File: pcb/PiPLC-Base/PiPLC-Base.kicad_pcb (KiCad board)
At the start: 2 copper layers, 158 x 85 mm, 144 parts, among them J1 WJ2EDGRC-5.08-4P, J10 WJ2EDGRC-5.08-4P, J11 WJ2EDGRC-5.08-4P, J12 WJ2EDGRC-5.08-4P, J13 ?, J2 KNX, J3 WJ2EDGRC-5.08-4P, J4 WJ2EDGRC-5.08-4P, J5 WJ2EDGRC-5.08-4P, J6 WJ2EDGRC-5.08-4P, J7 WJ2EDGRC-5.08-4P, J8 WJ2EDGRC-5.08-4P, J9 WJ2EDGRC-5.08-4P, J99 Rpi GPIO, K1 G5RL-1A-E-TV8 DC24, K2 G5RL-1A-E-TV8 DC24, K3 G5RL-1A-E-TV8 DC24, K4 G5RL-1A-E-TV8 DC24, K5 G5RL-1A-E-TV8 DC24, K6 G5RL-1A-E-TV8 DC24, K7 G5RL-1A-E-TV8 DC24, K8 G5RL-1A-E-TV8 DC24, Q1 AO3400A, Q2 AO3400A, Q3 AO3400A, Q4 AO3400A, Q5 AO3400A, Q6 AO3400A, Q7 AO3400A, Q8 AO3400A, U1 TPS54331D, U10 EL817C, U11 EL817C, U2 NCN5121, U3 ISO1540, U4 EL817C, U5 EL817C, U6 EL817C, U7 EL817C, U8 EL817C, U9 EL817C, Y1 16MHz

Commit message: Move stuff on both PCBs for 3D proof of concept
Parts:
- removed D10, D11, D20, D21, D22, D23, D24, D25, D26, D27, D4, D5, D6, D7, D8, D9: LED, LED_THT:LED_D5.0mm
- removed J2: KNX, MeineBib:KNX_Header
- moved C6 32.4 mm to (58.7, 143.3)
- moved C7 32.4 mm to (58.7, 146.6)
- moved C1 32.4 mm to (-9.28, 130.1)
- moved C10 32.4 mm to (49.9, 151.3)
- moved C11 32.4 mm to (-9.28, 147.7)
- moved C12 32.4 mm to (-9.28, 150.2)
- moved C13 32.4 mm to (-9.28, 152.7)
- moved C14 32.4 mm to (-5.27, 130.1)
- moved C15 32.4 mm to (24.3, 132.9)
- moved C16 32.4 mm to (24.2, 141.5)
- moved C2 32.4 mm to (-9.28, 132.6)
- moved C3 32.4 mm to (-9.28, 135.1)
- moved C4 32.4 mm to (-9.28, 137.6)
- moved C5 32.4 mm to (-9.28, 140.1)
- moved C8 32.4 mm to (-9.28, 142.7)
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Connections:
- net /GPIO_02 renamed I²C SDA
- net /GPIO_03 renamed I²C SCL
- net GND renamed KNX -
- net Net-(D2-A) renamed KNX +
- R16 pad 1: Net-(D4-A) -> /GPIO_09
- R16 pad 2: +3V3 -> LED_I5
- R17 pad 1: Net-(D5-A) -> /GPIO_11
- R17 pad 2: +3V3 -> LED_I6
- R18 pad 1: Net-(D6-A) -> /GPIO_05
- R18 pad 2: +3V3 -> LED_I7
- R19 pad 1: Net-(D7-A) -> /GPIO_06
- R19 pad 2: +3V3 -> LED_I8
- R20 pad 1: Net-(D8-A) -> /GPIO_17
- R20 pad 2: +3V3 -> LED_I1
- R21 pad 1: Net-(D9-A) -> /GPIO_27
- R21 pad 2: +3V3 -> LED_I2
- R22 pad 1: Net-(D10-A) -> /GPIO_22
- R22 pad 2: +3V3 -> LED_I3
- R23 pad 1: Net-(D11-A) -> /GPIO_10
- R23 pad 2: +3V3 -> LED_I4
- R25 pad 1: Net-(D21-A) -> LED_Q2
- R27 pad 1: Net-(D22-A) -> LED_Q3
- R30 pad 1: Net-(D23-A) -> LED_Q4
- R33 pad 1: Net-(D24-A) -> LED_Q5
- R36 pad 1: Net-(D25-A) -> LED_Q6
- R39 pad 1: Net-(D26-A) -> LED_Q7
- R42 pad 1: Net-(D27-A) -> LED_Q8
- R48 pad 1: Net-(D20-A) -> LED_Q1

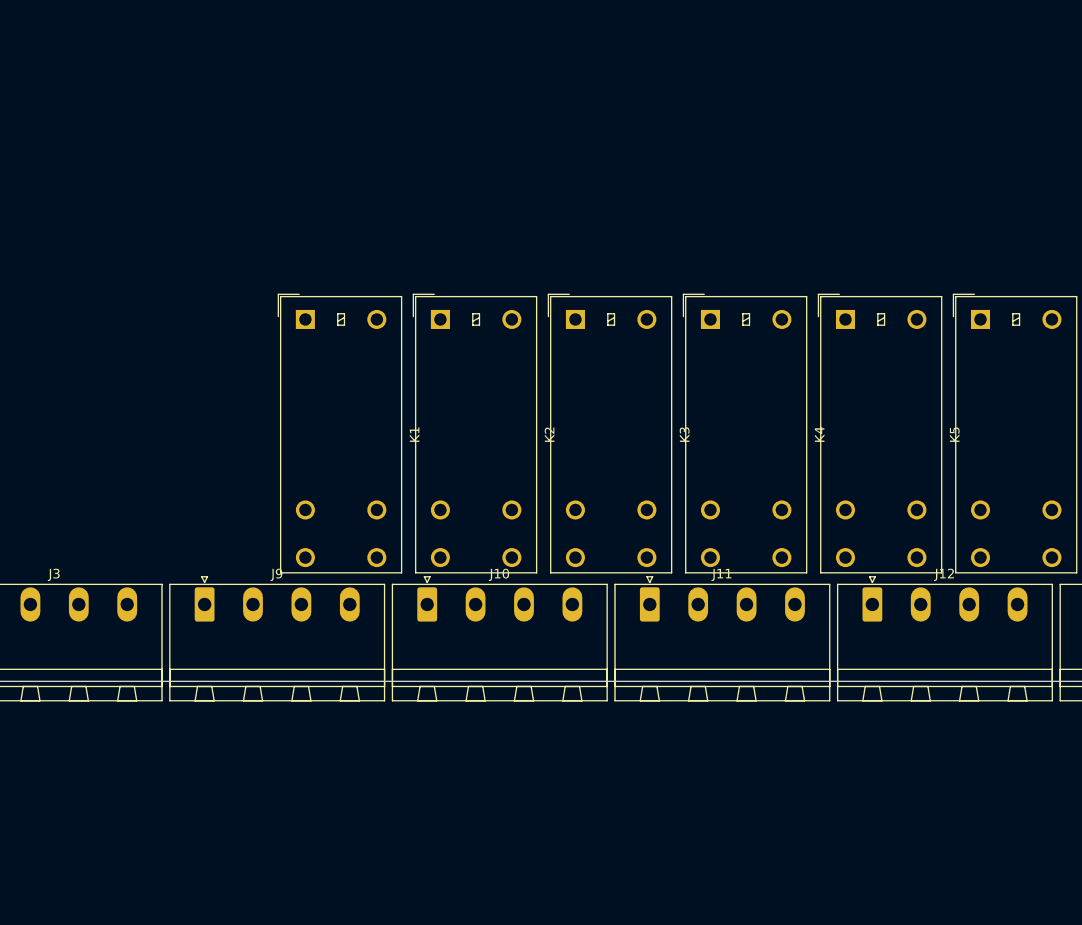
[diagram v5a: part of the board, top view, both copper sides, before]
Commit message: Add Modbus
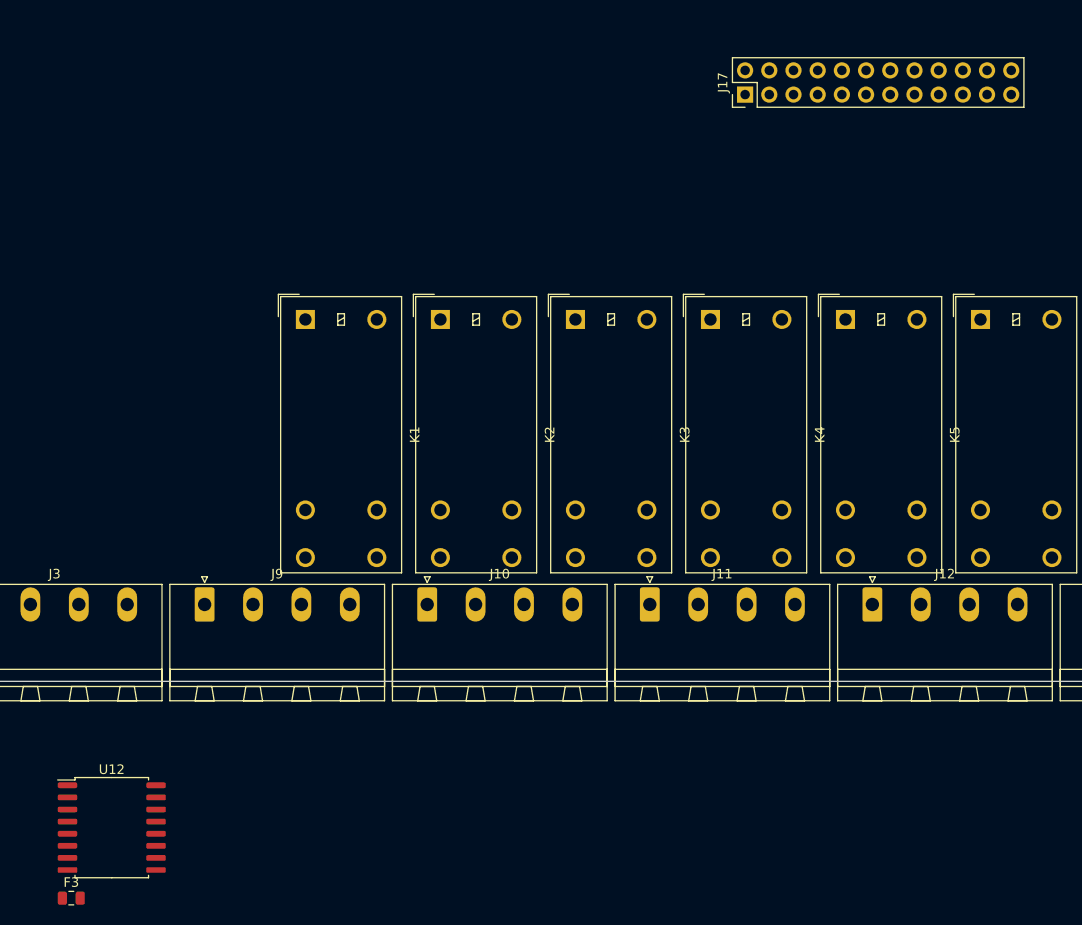
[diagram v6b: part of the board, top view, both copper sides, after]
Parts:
- added F3: 500mA, Fuse:Fuse_0805_2012Metric, F.Cu at (88.3, 171.3)
- added J17: Conn_02x12_Odd_Even, Connector_PinHeader_2.54mm:PinHeader_2x12_P2.54mm_Vertical, F.Cu at (159.0, 86.9)
- added U12: ISO3082DWR, Package_SO:SOIC-16W_7.5x10.3mm_P1.27mm, F.Cu at (92.5, 163.9)
- J13: value ? -> Modbus
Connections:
- J13 pad 1: /GPIO_13 -> Net-(J13-Pin_1)
- J13 pad 2: /GPIO_19 -> Net-(J13-Pin_2)
- J13 pad 3: /GPIO_23 -> Net-(J13-Pin_3)
- J13 pad 4: /GPIO_18 -> KNX -
- J5 pad 4: /GPIO_26 -> /1-Wire
- J99 pad 16: /GPIO_23 -> /1-Wire
- J99 pad 7: /1-Wire -> /GPIO_04
- R18 pad 1: /GPIO_05 -> /GPIO_13
- R19 pad 1: /GPIO_06 -> /GPIO_26
- U10 pad 4: /GPIO_05 -> /GPIO_13
- U11 pad 4: /GPIO_06 -> /GPIO_26

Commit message: Minor cleanup on main board
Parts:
- removed Y1: 16MHz, Crystal:Crystal_SMD_3225-4Pin_3.2x2.5mm
- added Y2: 16MHz, Crystal:Crystal_SMD_3225-4Pin_3.2x2.5mm, F.Cu at (25.7, 131.3)
- moved U12 74.3 mm to (39.6, 111.7)
- moved F3 74.3 mm to (35.3, 119.1)
- moved C10 13.8 mm to (36.4, 148.9)
- moved C14 13.8 mm to (-18.8, 127.7)
- moved C6 13.8 mm to (45.2, 140.8)
- moved C7 13.8 mm to (45.2, 144.2)
- moved D1 13.8 mm to (38.1, 70.0)
- moved D14 13.8 mm to (38.1, 92.8)
- moved D15 13.8 mm to (46.2, 70.0)
- moved D16 13.8 mm to (46.2, 74.5)
- moved D17 13.8 mm to (46.2, 79.1)
- moved D2 13.8 mm to (38.1, 74.5)
- moved D3 13.8 mm to (38.1, 79.1)
- moved F2 13.8 mm to (44.9, 135.7)
- moved L1 13.8 mm to (38.4, 135.2)
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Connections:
- C1 pad 2: KNX - -> GND
- C12 pad 2: KNX - -> GND
- C13 pad 2: KNX - -> GND
- C14 pad 2: KNX - -> GND
- C15 pad 2: KNX - -> GND
- C16 pad 2: KNX - -> GND
- C3 pad 2: KNX - -> GND
- C5 pad 2: KNX - -> GND
- C6 pad 2: KNX - -> GND
- C7 pad 2: KNX - -> GND
- C8 pad 2: KNX - -> GND
- C9 pad 2: KNX - -> GND
- D1 pad 2: KNX - -> GND
- D3 pad 1: KNX - -> GND
- J1 pad 1: +24V -> /GPIO_18
- J1 pad 2: KNX - -> /GPIO_19
- J1 pad 3: I²C SDA -> unconnected-(J1-Pin_3-Pad3)
- J1 pad 4: I²C SCL -> unconnected-(J1-Pin_4-Pad4)
- J13 pad 4: KNX - -> GND
- J17 pad 5: KNX - -> GND
- J17 pad 6: KNX - -> GND
- J3 pad 3: KNX - -> GND
- J3 pad 4: KNX - -> GND
- J4 pad 2: KNX - -> GND
- J5 pad 2: KNX - -> GND
- J99 pad 14: KNX - -> GND
- J99 pad 20: KNX - -> GND
- J99 pad 25: KNX - -> GND
- J99 pad 30: KNX - -> GND
- J99 pad 34: KNX - -> GND
- J99 pad 39: KNX - -> GND
- J99 pad 6: KNX - -> GND
- J99 pad 9: KNX - -> GND
- Q1 pad 2: KNX - -> GND
- Q2 pad 2: KNX - -> GND
- Q3 pad 2: KNX - -> GND
- Q4 pad 2: KNX - -> GND
- Q5 pad 2: KNX - -> GND
- Q6 pad 2: KNX - -> GND
- Q7 pad 2: KNX - -> GND
- Q8 pad 2: KNX - -> GND
- R1 pad 2: KNX - -> GND
- R24 pad 2: KNX - -> GND
- R29 pad 2: KNX - -> GND
- R32 pad 2: KNX - -> GND
- R35 pad 2: KNX - -> GND
- R38 pad 2: KNX - -> GND
- R4 pad 2: KNX - -> GND
- R41 pad 2: KNX - -> GND
- R44 pad 2: KNX - -> GND
- R47 pad 2: KNX - -> GND
- TP4 pad 1: KNX - -> GND
- U1 pad 7: KNX - -> GND
- U10 pad 2: KNX - -> GND
- U10 pad 3: KNX - -> GND
- U11 pad 2: KNX - -> GND
- U11 pad 3: KNX - -> GND
- U12 pad 10: KNX - -> GND
- U12 pad 15: KNX - -> GND
- U12 pad 2: KNX - -> GND
- U12 pad 7: KNX - -> GND
- U12 pad 8: KNX - -> GND
- U12 pad 9: KNX - -> GND
- U2 pad 1: KNX - -> GND
- U2 pad 14: KNX - -> GND
- U2 pad 18: KNX - -> GND
- U2 pad 2: KNX - -> GND
- U2 pad 23: KNX - -> GND
- U2 pad 24: KNX - -> GND
- U2 pad 25: KNX - -> GND
- U2 pad 31: KNX - -> GND
- U2 pad 33: KNX - -> GND
- U2 pad 38: KNX - -> GND
- U2 pad 41: (no net) -> GND
- U3 pad 4: KNX - -> GND
- U3 pad 5: KNX - -> GND
- U4 pad 2: KNX - -> GND
- U4 pad 3: KNX - -> GND
- U5 pad 2: KNX - -> GND
- U5 pad 3: KNX - -> GND
- U6 pad 2: KNX - -> GND
- U6 pad 3: KNX - -> GND
- U7 pad 2: KNX - -> GND
- U7 pad 3: KNX - -> GND
- U8 pad 2: KNX - -> GND
- U8 pad 3: KNX - -> GND
- U9 pad 2: KNX - -> GND
- U9 pad 3: KNX - -> GND

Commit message: Add decoupling / filtering to all IC's and relays
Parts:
- added C17: 100uF, Capacitor_SMD:CP_Elec_6.3x7.7, F.Cu at (7.95, 113.5)
- added C18: 100nF, Capacitor_SMD:C_0603_1608Metric, F.Cu at (0.71, 110.7)
- added C19: 100nF, Capacitor_SMD:C_0603_1608Metric, F.Cu at (0.71, 113.2)
- added C20: 100nF, Capacitor_SMD:C_0603_1608Metric, F.Cu at (0.71, 115.7)
- added C21: 100nF, Capacitor_SMD:C_0603_1608Metric, F.Cu at (0.71, 118.2)
